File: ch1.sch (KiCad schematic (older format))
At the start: 49 parts, among them J1 CH1, J3 CH1OUT, Q101 BC856BDW1, Q102 LS844, Q103 BC846BDW1, Q104 BC856, Q105 BCP53, Q106 BC846, Q107 BCP56, Q111 BC856BDW1, Q112 LS844, Q113 BC846BDW1, Q114 BC856, Q115 BCP53, Q116 BC846, Q117 BCP56

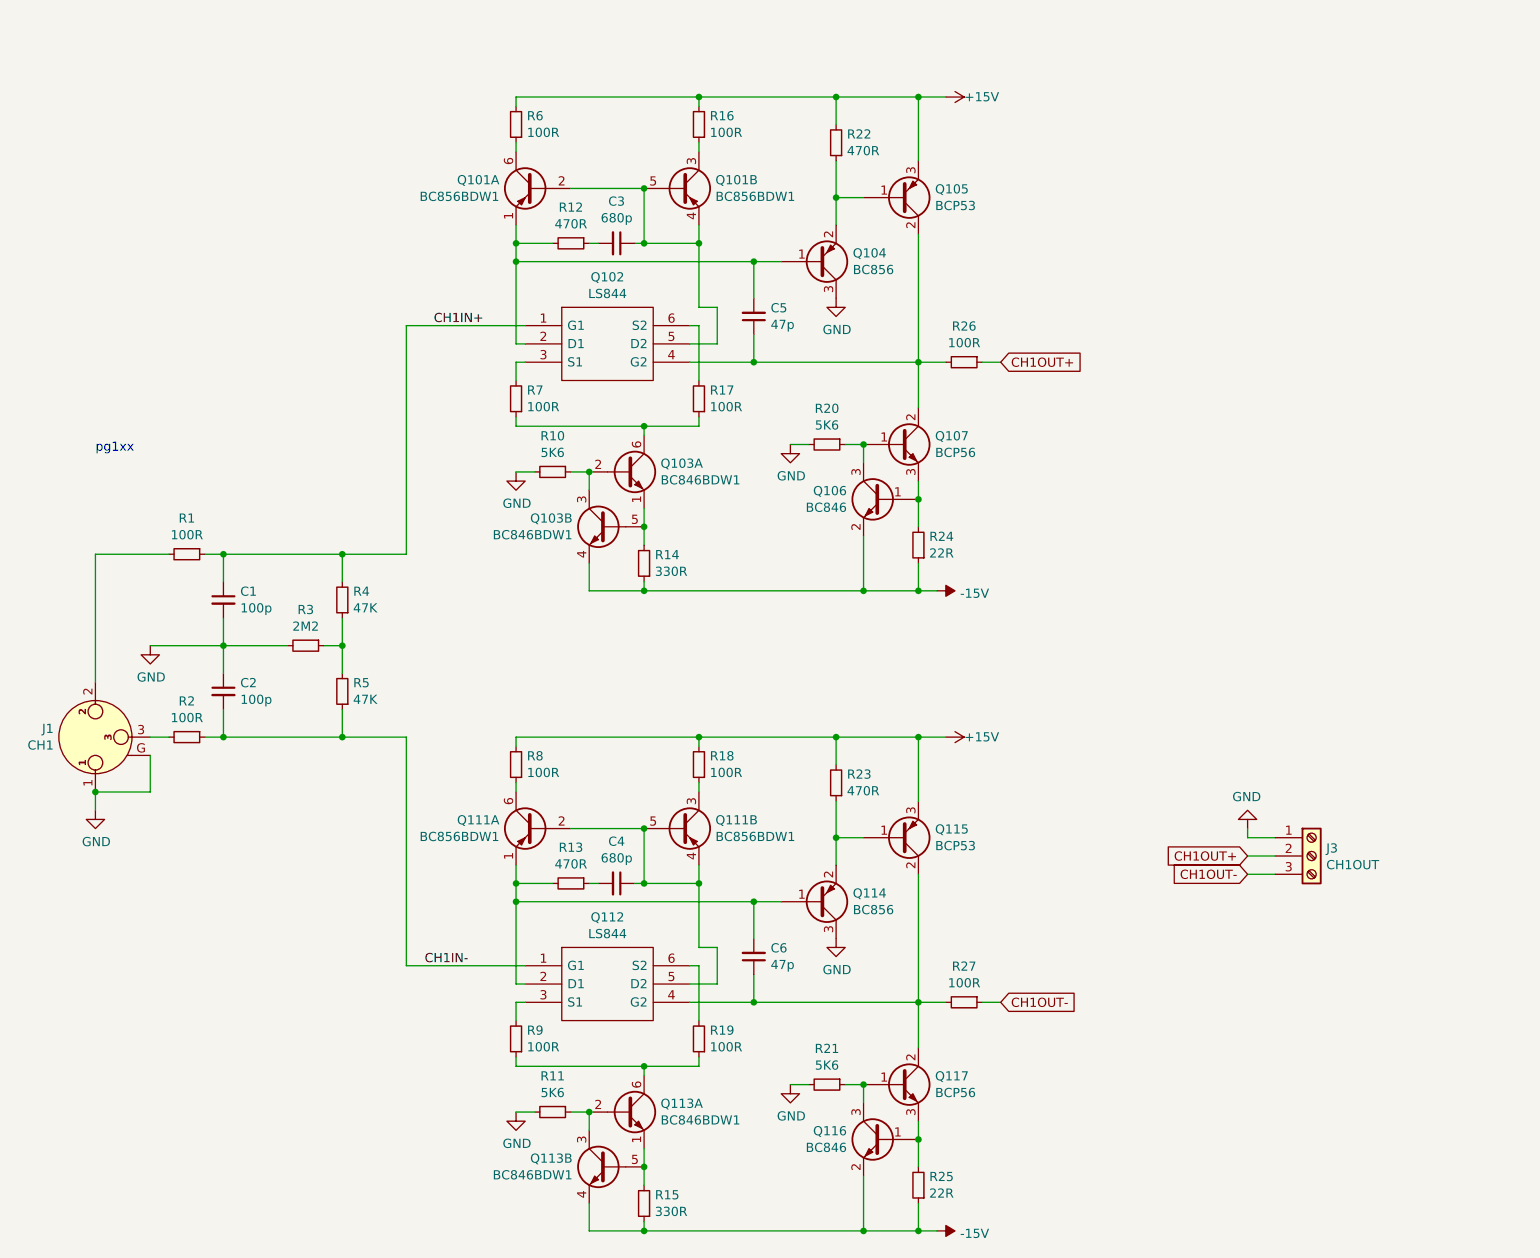
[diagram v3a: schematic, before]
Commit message: started pcb layout
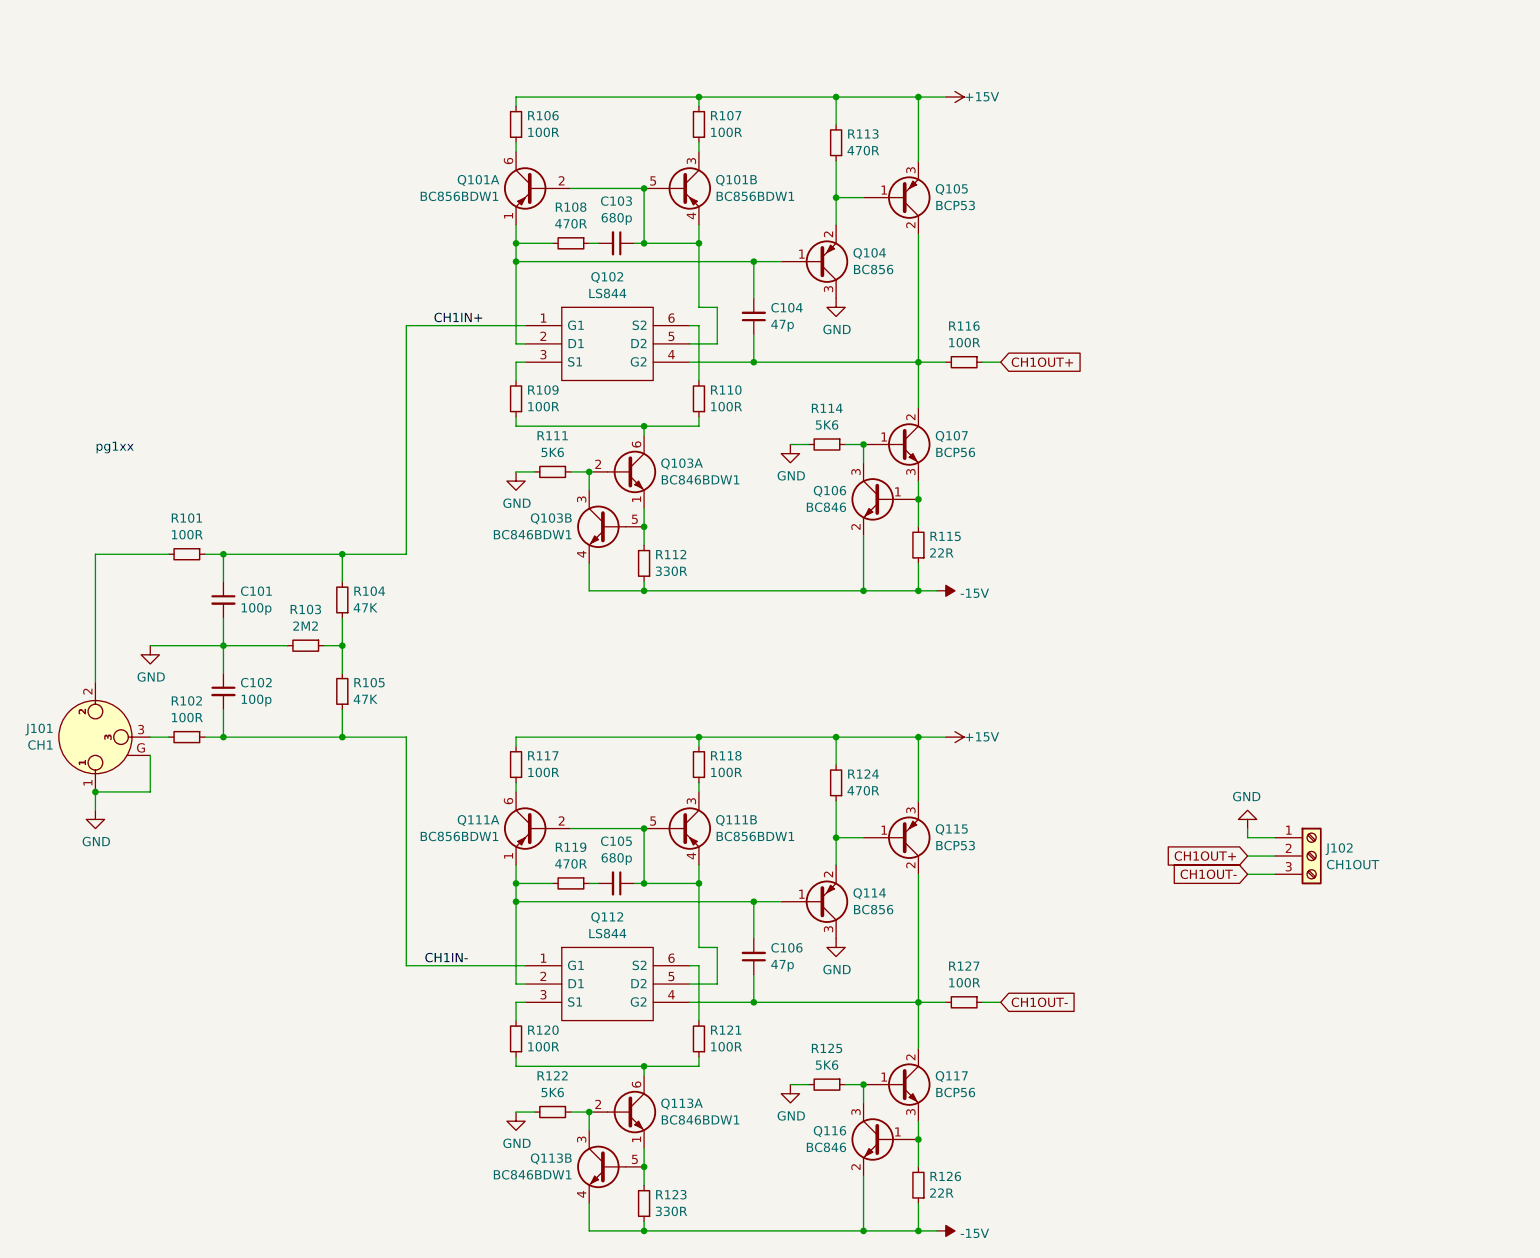
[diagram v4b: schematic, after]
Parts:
- renumbered C1 to C101, C2 to C102, C3 to C103, C5 to C104, C4 to C105, C6 to C106, J1 to J101, J3 to J102, R1 to R101, R2 to R102, R3 to R103, R4 to R104, R5 to R105, R6 to R106, R16 to R107, R12 to R108, R7 to R109, R17 to R110, R10 to R111, R14 to R112, R22 to R113, R20 to R114, R24 to R115, R26 to R116, R8 to R117, R18 to R118, R13 to R119, R9 to R120, R19 to R121, R11 to R122, R15 to R123, R23 to R124, R21 to R125, R25 to R126, R27 to R127

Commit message: pcb started
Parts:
- removed C103, C105: 680p, Capacitor_SMD:C_0805_2012Metric_Pad1.15x1.40mm_HandSolder, symbol Device:C_Small
- removed R108, R119: 470R, Resistor_SMD:R_0805_2012Metric_Pad1.15x1.40mm_HandSolder, symbol Device:R_Small
- removed R116, R127: 100R, Resistor_SMD:R_0805_2012Metric_Pad1.15x1.40mm_HandSolder, symbol Device:R_Small
- added C101, C102: 10u, Capacitor_THT:C_Radial_D5.0mm_H7.0mm_P2.00mm, symbol Device:C_Small
- C105: renamed from C104; value 47p -> 27p
- C106: value 47p -> 27p
- renumbered C101 to C103, C102 to C104, R109 to R108, R110 to R109, R111 to R110, R112 to R111, R113 to R112, R114 to R113, R115 to R114, R117 to R115, R118 to R116, R120 to R117, R121 to R118, R122 to R119, R123 to R120, R124 to R121, R125 to R122, R126 to R123
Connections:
- net CH1OUT+: now also C105.1, Q102.4 (G2), Q105.2 (C), Q105.4 (C), Q107.2 (C), Q107.4 (C)
- net CH1OUT-: now also C106.1, Q112.4 (G2), Q115.2 (C), Q115.4 (C), Q117.2 (C), Q117.4 (C)
- net at J101.2: now also C101.2; no longer R101.2
- net at J101.3: now also C102.2; no longer R102.2
- net CH1+_FB: now reaches C105.2, Q101.1 (E1), Q102.2 (D1), Q104.1 (B)
- net CH1-_FB: now reaches C106.2, Q111.1 (E1), Q112.2 (D1), Q114.1 (B)
- new net: C101.1, R101.2
- new net: C102.1, R102.2
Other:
- moved on the sheet: C103, C104, C105, C106, J101, J102, Q101A, Q101B, Q102, Q103A, Q103B, Q104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
